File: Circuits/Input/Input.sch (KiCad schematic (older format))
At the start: 9 parts, among them J1 sensor, P1 WRITER-VCC, SW1 MKA-10110, U1 TWELITE_SMD

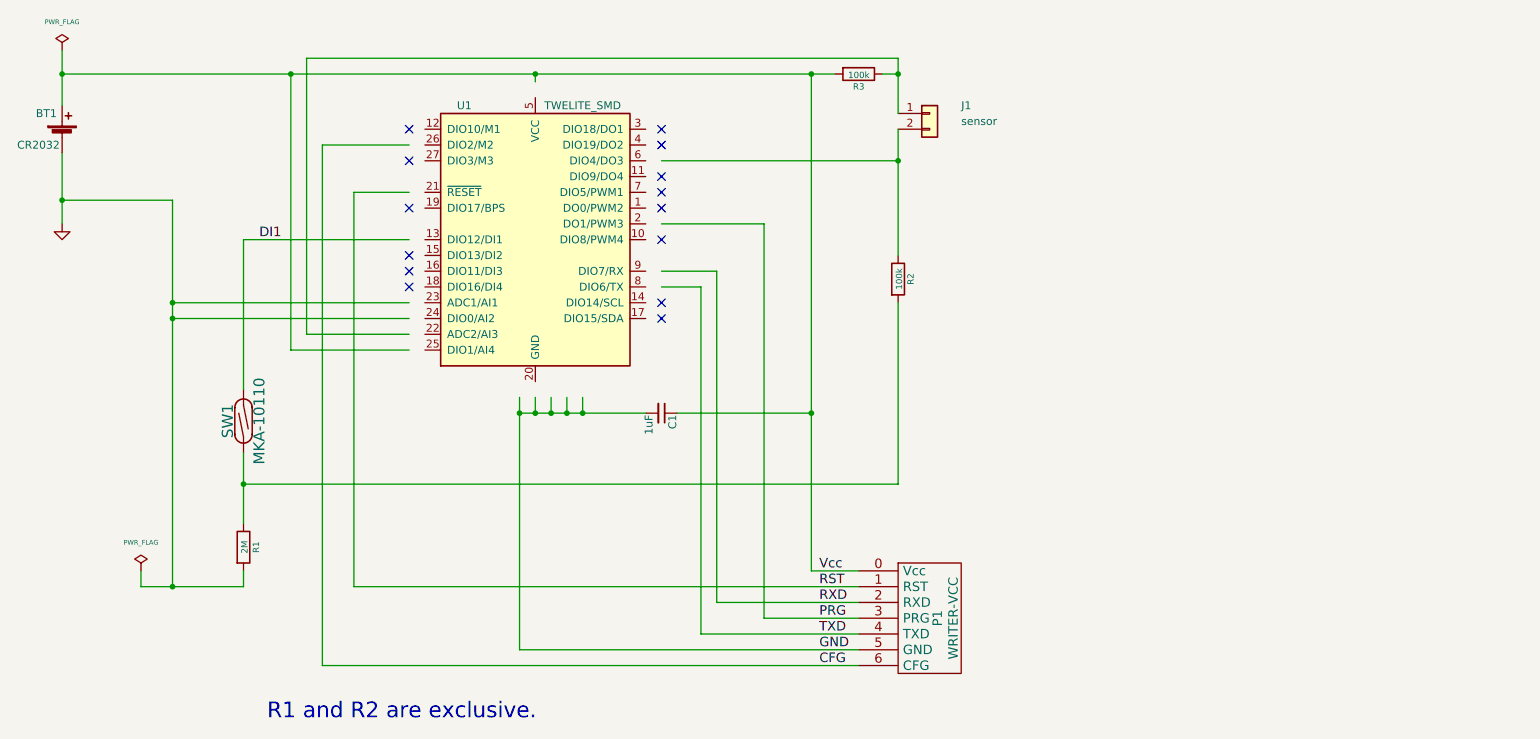
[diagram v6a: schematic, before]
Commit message: ADC2をGNDに配線
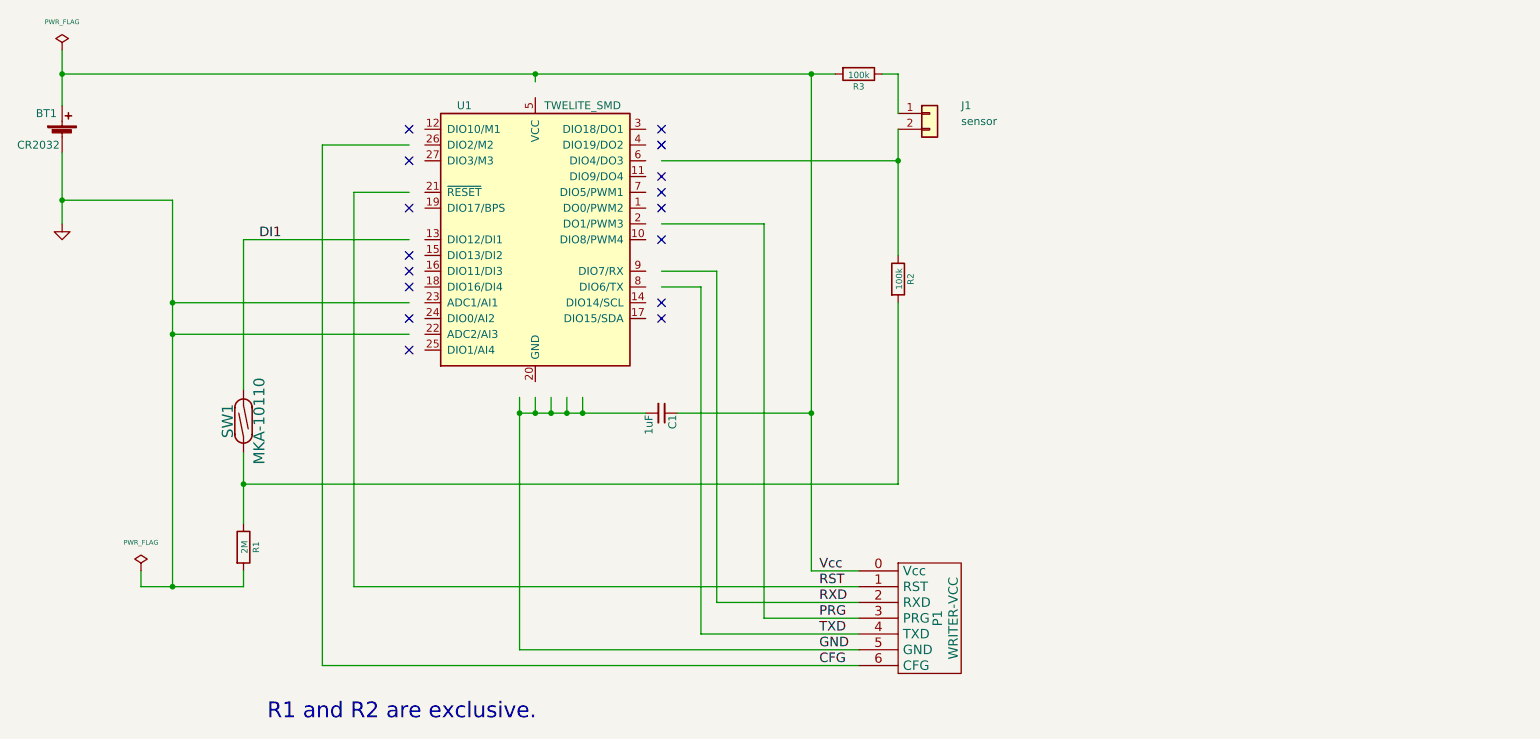
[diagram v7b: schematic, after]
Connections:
- wire segments 67 -> 60
- no-connect marks 14 -> 16
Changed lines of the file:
@@
 	1    0    0    -1
 $EndComp
-Wire Wire Line
-	6550 1300 2800 1300
-Wire Wire Line
-	2800 1300 2800 3050
 Connection ~ 6000 1400
 Wire Wire Line
@@
 Wire Wire Line
 	5050 1950 6550 1950
-Connection ~ 1950 2950
-Wire Wire Line
-	1950 2950 3450 2950
 Wire Wire Line
 	1250 2200 1950 2200
@@
 	1250 1900 1250 2200
 Wire Wire Line
-	2700 1400 2700 3150
-Wire Wire Line
 	6000 4550 6300 4550
-Wire Wire Line
-	1250 1400 2700 1400
 Wire Wire Line
 	3450 2150 3100 2150
@@
 Wire Wire Line
 	2400 2450 3450 2450
-Wire Wire Line
-	2700 3150 3450 3150
 Wire Wire Line
 	3450 1850 2900 1850
@@
 Wire Wire Line
 	6450 1400 6550 1400
-Connection ~ 6550 1400
 Wire Wire Line
 	6550 1650 6550 1400
 Wire Wire Line
 	6000 1400 6150 1400
-Wire Wire Line
-	1950 2950 1950 4650
 Wire Wire Line
 	1250 1400 1250 1600
@@
 	1950 4650 2400 4650
 Wire Wire Line
-	1950 2850 1950 2950
-Wire Wire Line
 	6550 1950 6550 2550
 Wire Wire Line
 	2400 4000 2400 4250
 Wire Wire Line
-	6550 1400 6550 1300
-Wire Wire Line
 	2900 5150 6300 5150
 Wire Wire Line
 	4150 3450 4150 3550
-Connection ~ 2700 1400
-Wire Wire Line
-	2700 1400 4250 1400
 NoConn ~ 5050 1750
 NoConn ~ 5050 1850
@@
 NoConn ~ 5050 2450
 NoConn ~ 3450 2250
-Wire Wire Line
-	3450 3050 2800 3050
 NoConn ~ 3450 2550
 NoConn ~ 3450 2650
@@
 $EndComp
 $Comp
-L power:PWR_FLAG #FLG?
+L power:PWR_FLAG #FLG0101
 U 1 1 5AAF2C2D
 P 1750 4550
-F 0 "#FLG?" H 1750 4645 30  0001 C CNN
+F 0 "#FLG0101" H 1750 4645 30  0001 C CNN
 F 1 "PWR_FLAG" H 1750 4730 30  0000 C CNN
 F 2 "" H 1750 4550 60  0000 C CNN
@@
 	1750 4650 1950 4650
 Connection ~ 1950 4650
+Wire Wire Line
+	1950 2850 1950 3050
+Wire Wire Line
+	3450 3050 1950 3050
+Connection ~ 1950 3050
+Wire Wire Line
+	1950 3050 1950 4650
+Wire Wire Line
+	1250 1400 4250 1400
+NoConn ~ 3450 2950
+NoConn ~ 3450 3150
 $EndSCHEMATC

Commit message: Updated symbol of TWELITE
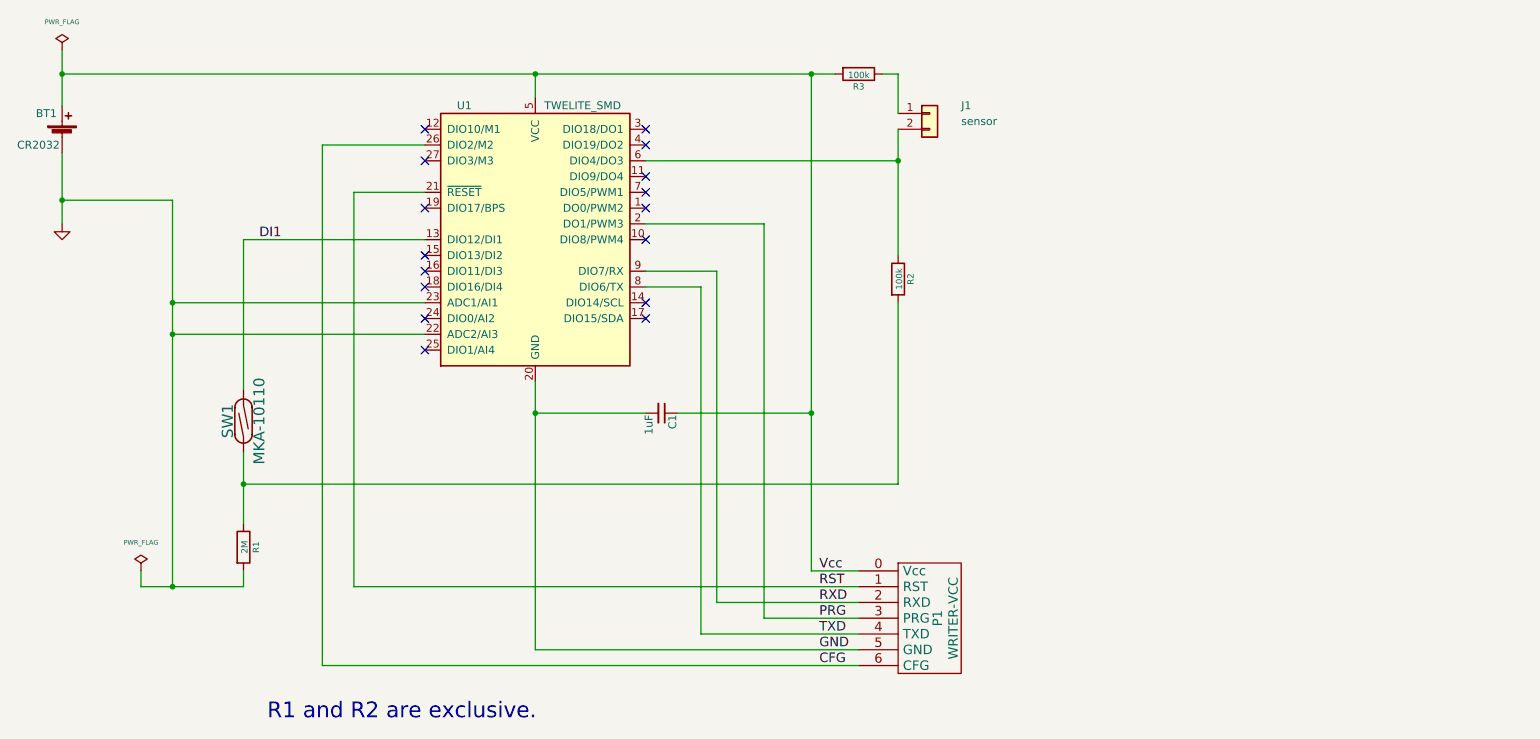
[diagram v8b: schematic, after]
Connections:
- wire segments 60 -> 52
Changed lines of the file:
@@
 	1    0    0    -1
 $EndComp
-NoConn ~ 3450 1750
+NoConn ~ 3550 1750
 Text Label 2500 2450 0    60   ~ 0
 DI1
-NoConn ~ 3450 1950
+NoConn ~ 3550 1950
 Text Label 6050 4650 0    60   ~ 0
 RST
@@
 	6550 1750 6550 1950
 Wire Wire Line
-	5050 1950 6550 1950
+	4950 1950 6550 1950
 Wire Wire Line
 	1250 2200 1950 2200
@@
 	6000 4550 6300 4550
 Wire Wire Line
-	3450 2150 3100 2150
+	3550 2150 3100 2150
 Wire Wire Line
 	3100 2150 3100 4650
 Wire Wire Line
-	5050 2350 5700 2350
+	4950 2350 5700 2350
 Wire Wire Line
 	2900 1850 2900 5150
@@
 	2400 3400 2400 2450
 Wire Wire Line
-	2400 2450 3450 2450
-Wire Wire Line
-	3450 1850 2900 1850
+	2400 2450 3550 2450
+Wire Wire Line
+	3550 1850 2900 1850
 Wire Wire Line
 	2400 4650 2400 4550
@@
 	1950 2200 1950 2850
 Wire Wire Line
-	3450 2850 1950 2850
+	3550 2850 1950 2850
 Connection ~ 1950 2850
 Wire Wire Line
@@
 	2900 5150 6300 5150
 Wire Wire Line
-	4150 3450 4150 3550
-NoConn ~ 5050 1750
-NoConn ~ 5050 1850
-NoConn ~ 5050 2050
-NoConn ~ 5050 2850
-NoConn ~ 5050 2950
-Wire Wire Line
-	4150 5050 6300 5050
+	4250 3350 4250 3550
+NoConn ~ 4950 1750
+NoConn ~ 4950 1850
+NoConn ~ 4950 2050
+NoConn ~ 4950 2850
+NoConn ~ 4950 2950
+Wire Wire Line
+	4250 5050 6300 5050
 Wire Wire Line
 	5700 2350 5700 4850
@@
 $EndComp
 Wire Wire Line
-	5050 2750 5300 2750
+	4950 2750 5300 2750
 Wire Wire Line
 	5300 2750 5300 4950
@@
 	5300 4950 6300 4950
 Wire Wire Line
-	5050 2650 5400 2650
+	4950 2650 5400 2650
 Wire Wire Line
 	5400 2650 5400 4750
 Wire Wire Line
 	5400 4750 6300 4750
-NoConn ~ 5050 2150
-NoConn ~ 5050 2250
-NoConn ~ 5050 2450
-NoConn ~ 3450 2250
-NoConn ~ 3450 2550
-NoConn ~ 3450 2650
-NoConn ~ 3450 2750
-Wire Wire Line
-	4250 1450 4250 1400
+NoConn ~ 4950 2150
+NoConn ~ 4950 2250
+NoConn ~ 4950 2450
+NoConn ~ 3550 2250
+NoConn ~ 3550 2550
+NoConn ~ 3550 2650
+NoConn ~ 3550 2750
+Wire Wire Line
+	4250 1550 4250 1400
 Connection ~ 4250 1400
 Wire Wire Line
 	4250 1400 6000 1400
-Wire Wire Line
-	4550 3450 4550 3550
-Wire Wire Line
-	4550 3550 4450 3550
-Connection ~ 4150 3550
-Wire Wire Line
-	4250 3450 4250 3550
 Connection ~ 4250 3550
 Wire Wire Line
-	4250 3550 4150 3550
-Wire Wire Line
-	4350 3450 4350 3550
-Connection ~ 4350 3550
-Wire Wire Line
-	4350 3550 4250 3550
-Wire Wire Line
-	4450 3450 4450 3550
-Connection ~ 4450 3550
-Wire Wire Line
-	4450 3550 4350 3550
-Wire Wire Line
-	4950 3550 4550 3550
-Wire Wire Line
-	4150 3550 4150 5050
+	4250 3550 4250 5050
 Wire Wire Line
 	6000 3550 6000 4550
@@
 Wire Wire Line
 	2400 4000 6550 4000
-Connection ~ 4550 3550
 Connection ~ 1250 1400
 Wire Wire Line
@@
 	1950 2850 1950 3050
 Wire Wire Line
-	3450 3050 1950 3050
+	3550 3050 1950 3050
 Connection ~ 1950 3050
 Wire Wire Line
@@
 Wire Wire Line
 	1250 1400 4250 1400
-NoConn ~ 3450 2950
-NoConn ~ 3450 3150
+NoConn ~ 3550 2950
+NoConn ~ 3550 3150
+Wire Wire Line
+	4250 3550 4950 3550
 $EndSCHEMATC
